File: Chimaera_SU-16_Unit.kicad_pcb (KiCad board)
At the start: 2 copper layers, 80 x 30 mm, 67 parts, among them P0 CONN_4, P1 CONN_4, P2 CONN_3, U0 CD74HC4067, U1 MCP602, U2 MCP1703

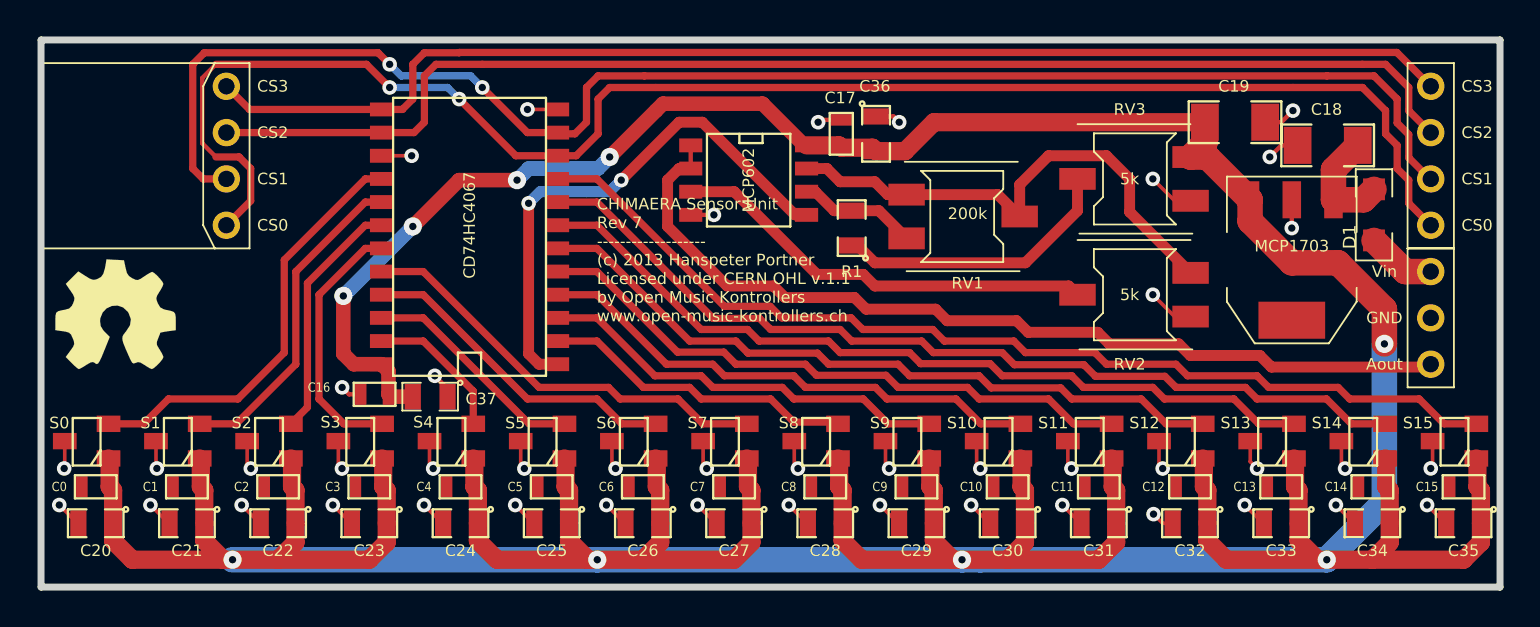
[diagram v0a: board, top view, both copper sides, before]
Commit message: 0.9mm (elliptical) pad holes, 0.8x0.2mm text size
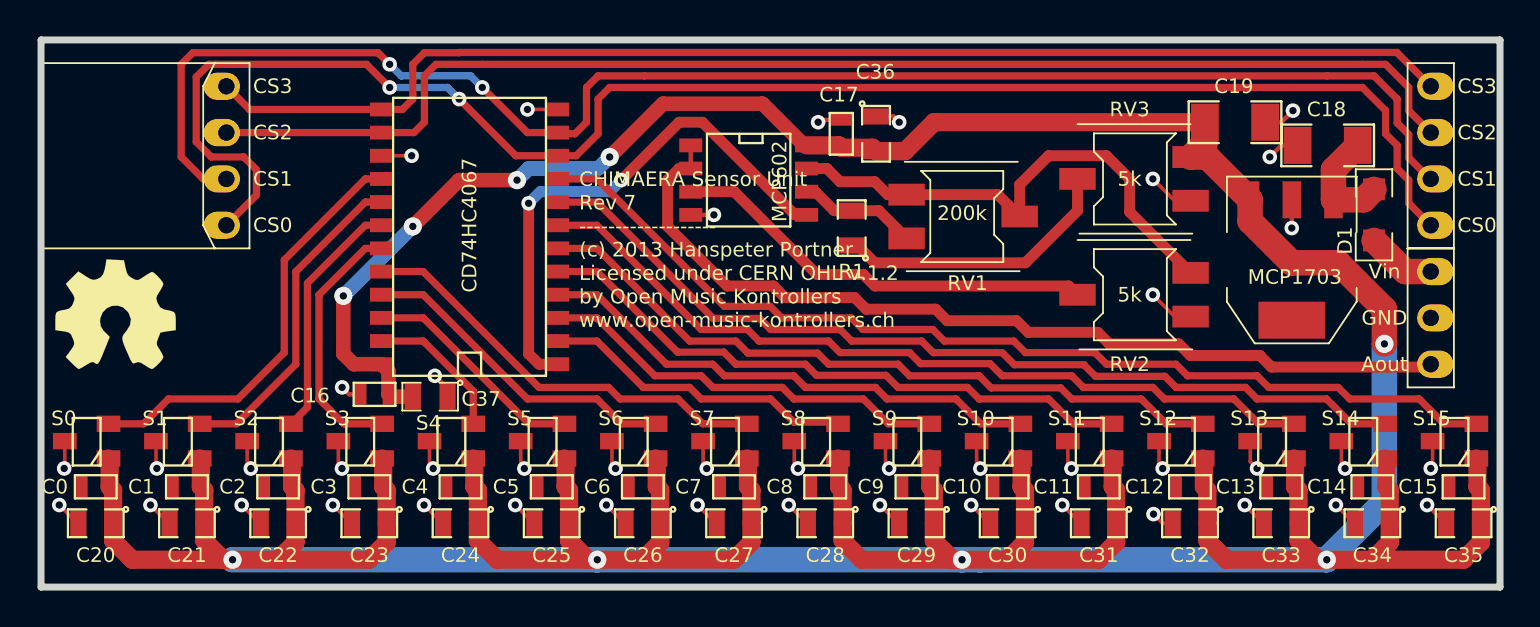
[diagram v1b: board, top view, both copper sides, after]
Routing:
- net N-0000010: track 88.2 -> 89.3 mm
- net N-0000018: track 84.1 -> 85.0 mm
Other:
- board text added: "CHIMAERA Sensor Unit Rev 7 ------------------- (c) 2013 Hanspeter Portner Licensed under CERN OHL v.1.2 by Open Music Kontrollers www.open-music-kontrollers.ch"
- board text removed: "CHIMAERA Sensor Unit Rev 7 ------------------- (c) 2013 Hanspeter Portner Licensed under CERN OHL v.1.1 by Open Music Kontrollers www.open-music-kontrollers.ch"
